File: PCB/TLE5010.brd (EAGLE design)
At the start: 73.3 x 17.8 mm, 10 parts, among them U1 TLE5010

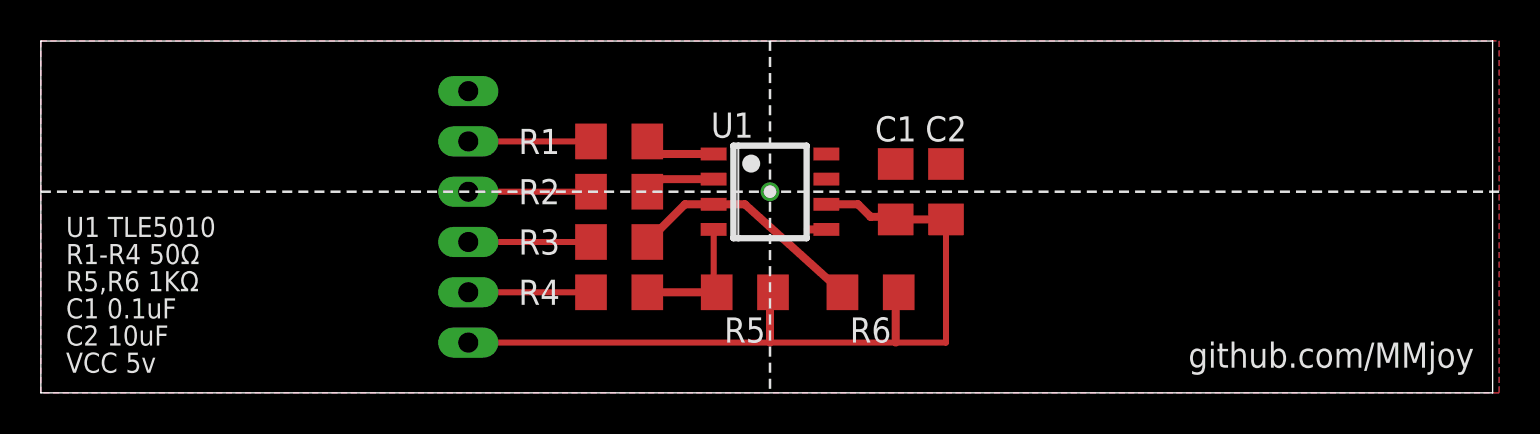
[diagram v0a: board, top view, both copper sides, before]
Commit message: Fixed J1 orientation
now corresponds with Cougar MMjoy board headers
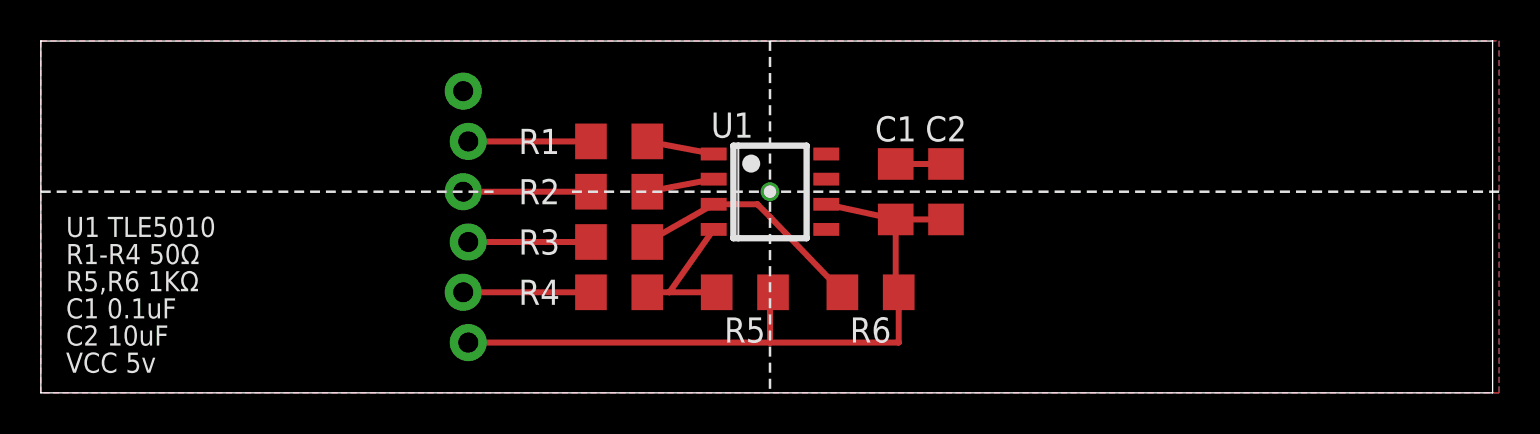
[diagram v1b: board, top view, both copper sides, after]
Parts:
- J1: device con-lstb:MA06-1 -> SparkFun-Connectors:MOLEX-1X6_LOCK
- moved J1 6.35 mm to (21.6, 2.54)
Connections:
- net N$11 renamed MISO
- net N$3 renamed CLK
- net N$4 renamed SCK
- net N$5 renamed CS
- net N$7 renamed DATA
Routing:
- net VCC: track 42.1 -> 36.8 mm
- net GND: track 1.65 -> 2.57 mm
- net DATA: track 6.83 -> 7.61 mm
- net N$2: track 3.99 -> 3.41 mm
- net N$1: track 3.99 -> 3.41 mm
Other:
- board text added: "BY NC SA"
- board text added: "MISO"
- board text added: "github.com/mejtoogood/TLE5010"
- board text removed: "DATA"
- board text removed: "NC SA"
- board text removed: "github.com/MMjoy"
